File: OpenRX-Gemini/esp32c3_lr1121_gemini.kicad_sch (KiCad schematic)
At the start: 42 parts, among them T1 0900PC16J0042001E, U1 ESP32-C3FH4, U2 TLV75533PDQNR, U3 RFX2401C, U4 LR1121IMLTRT, U5 OW2EL89CENUXFMYLC-32M, X1 CJ17-400001010B20

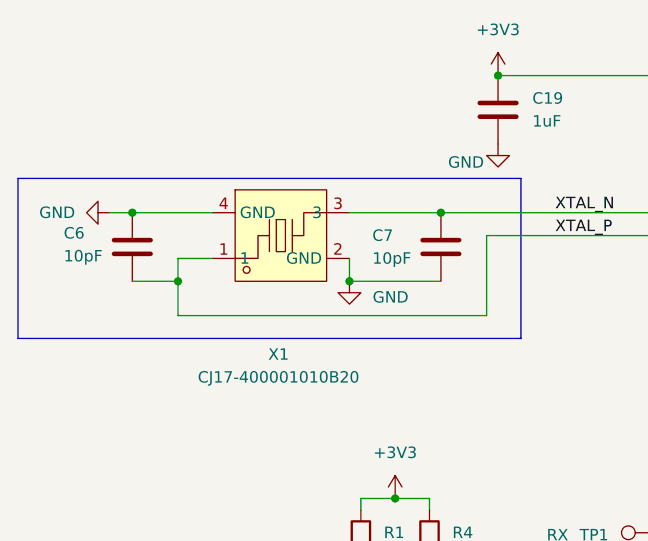
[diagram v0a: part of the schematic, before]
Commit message: Fix Gemini crystal load caps to 18pF (C62164), matching Lite and Mono
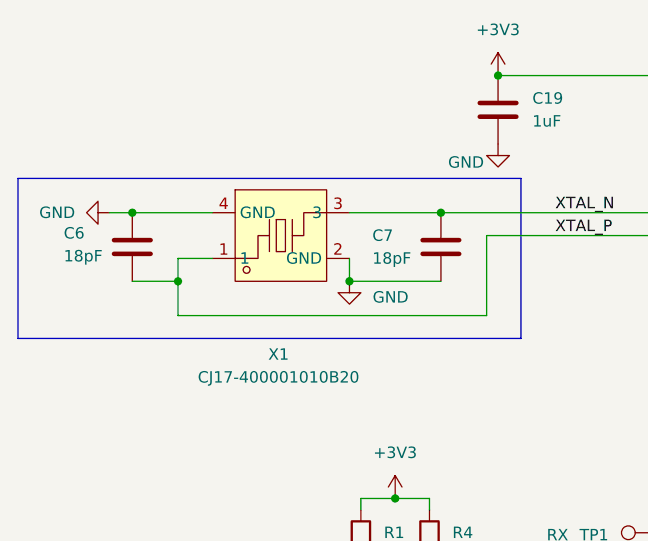
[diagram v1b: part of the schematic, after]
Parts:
- C1, C2, C21, C22, C23, C24, C3, C4, C5: LCSC C14858 -> C76939
- C10, C19, C26, C8, C9: LCSC C77857 -> C76935
- C25: LCSC C14856 -> C62548
- C6, C7: value 10pF -> 18pF; LCSC C14854 -> C62164
- L1: LCSC C1035 -> C6808014
- R1, R2, R3, R4: LCSC C172043 -> C106225
- R5: LCSC C25741 -> C270364

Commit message: OpenRX-Gemini: dual LR1121 schematic complete, 0 ERC errors
- Radio 1 (U4): sub-GHz via Johanson IPD → JP1 UFL
- Radio 2 (U9): 2.4GHz via RFX2401C (U10) → DEA (USB2) → JP3 UFL
- Shared SPI bus (SCK/MISO/MOSI), separate NSS/IRQ/BUSY/RST per radio
- Radio 2 control: GPIO10=NSS2, GPIO9=IRQ2, GPIO1=BUSY2, GPIO0=RST2
- FEM driven by Radio 2 RFSW (DIO5→RXEN, DIO6→TXEN)
- Radio 1 DIO5/DIO6 have 100k pull-downs (disconnected from FEM)
- No LED (GPIO10 used for NSS2), no boot button (GPIO9 used for IRQ2)
- Still needs: 10k pull-up on NSS2
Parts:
- removed C25: 220pF, Capacitor_SMD:C_0201_0603Metric, symbol Device:C
- removed C26: 1uF, Capacitor_SMD:C_0201_0603Metric, symbol Device:C
- removed D1: XL-1010RGBC-WS2812B, OpenRX-Shared:LED-SMD_4P-L1.0-W1.0-TL_XL-1010RGBC-WS2812B, symbol OpenRX-Shared:XL-1010RGBC-WS2812B
- removed JP2: U.FL-R-SMT-1(80), OpenRX-Shared:RF-SMD_FRF05002-JSS103M, symbol OpenRX-Shared:U.FL-R-SMT-1(80)
- removed U3: RFX2401C, OpenRX-Shared:QFN-16_L3.0-W3.0-P0.50-BL-EP1.7, symbol OpenRX-Shared:RFX2401C
- removed USB1: DEA102700LT-6307A2, OpenRX-Shared:FILTER-SMD_4P-L1.0-W0.5-L_DEA102700LT-XXX, symbol OpenRX-Shared:DEA102700LT-6307A2
- added C13, C38: 10pF, Capacitor_SMD:C_0201_0603Metric, symbol Device:C
- added C35, C36, C37, C40: 100nF, Capacitor_SMD:C_0201_0603Metric, symbol Device:C
- added C39: 4.7uF, Capacitor_SMD:C_0402_1005Metric, symbol Device:C
- added C41: 220pF, Capacitor_SMD:C_0201_0603Metric, symbol Device:C
- added C42: 1uF, Capacitor_SMD:C_0201_0603Metric, symbol Device:C
- added JP3: U.FL-R-SMT-1(80), OpenRX-Shared:RF-SMD_FRF05002-JSS103M, symbol OpenRX-Shared:U.FL-R-SMT-1(80)
- added L2: 24nH, Inductor_SMD:L_0201_0603Metric, symbol Device:L
- added L4: 10uH, Inductor_SMD:L_0603_1608Metric, symbol Device:L
- added R12, R6: 220R, Resistor_SMD:R_0201_0603Metric, symbol Device:R
- added R13, R14, R15, R16, R7: 100k, Resistor_SMD:R_0201_0603Metric, symbol Device:R
- added U10: RFX2401C, OpenRX-Shared:QFN-16_L3.0-W3.0-P0.50-BL-EP1.7, symbol OpenRX-Shared:RFX2401C
- added U8: OW2EL89CENUXFMYLC-32M, OpenRX-Shared:OSC-SMD_4P-L3.2-W2.5-BL, symbol OpenRX-Shared:OW2EL89CENUXFMYLC-32M
- added U9: LR1121IMLTRT, OpenRX-Shared:QFN-32_L5.0-W5.0-P0.50-BL-EP3.7, symbol OpenRX-Shared:LR1121IMLTRT
- added USB2: DEA102700LT-6307A2, OpenRX-Shared:FILTER-SMD_4P-L1.0-W0.5-L_DEA102700LT-XXX, symbol OpenRX-Shared:DEA102700LT-6307A2
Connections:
- net +3V3: now also C35.1, C40.2, C41.1, C42.1, L4.2, U10.14 (VDD), U10.16 (VDD), U9.15 (VBAT), U9.2 (VBAT_RF)
- net GND: now also C35.2, C36.1, C39.2, C40.1, C41.2, C42.2, JP3.2 (GND), JP3.3 (GND), R13.1, R14.1, R15.1, R16.1, R7.1, U10.1 (GND), U10.11 (GND), U10.12 (GND), U10.15 (GND), U10.17 (EP), U10.2 (GND), U10.3 (GND), U10.7 (GND), U10.8 (GND), U10.9 (GND), U8.1 (GND), U8.2 (GND), U9.13 (GND), U9.33 (EP), USB2.2 (GND), USB2.4 (GND)
- net MISO: now also U9.21 (DIO4)
- net MOSI: now also U9.22 (DIO3)
- net RXEN: now also U10.6 (RXEN), U9.20 (DIO5); no longer U4.20 (DIO5)
- net SCK: now also U9.23 (DIO2)
- net TXEN: now also U10.5 (TXEN), U9.19 (DIO6); no longer U4.19 (DIO6)
- net XTAL_P: now also L2.2; no longer C6.1, X1.1
- net RST2: now reaches U1.4 (XTAL_32K_P)
- net RST2: now also U9.6 (NRESET)
- net BUSY2: now reaches U1.5 (XTAL_32K_N)
- net BUSY2: now also U9.25 (DIO0/BUSY)
- net at U4.11 (DIO7): now also R7.2
- net at U5.3 (OUTPUT): now also R6.2; no longer U4.4 (XTA)
- net CHIP_BOOT renamed IRQ
- net IRQ: now also U9.9 (DIO9)
- net LED renamed NSS2
- net NSS2: now also U9.24 (DIO1)
- new net: C39.1, U9.1 (VR_PA)
- new net: C13.1, R6.1
- new net: U10.10 (ANT), USB2.1 (IN)
- new net: JP3.1 (SIG), USB2.3 (OUT)
- new net: R12.2, U8.3 (OUTPUT)
- new net: C37.1, U8.4 (VDD)
- new net: C6.1, L2.1, X1.1
- new net: R13.2, U9.11 (DIO7)
- new net: L4.1, U9.14 (DCC_SW)
- new net: C38.1, R12.1
- new net: U10.4 (TXRX), U9.26 (RFIO_HF)
- new net: C37.2, U9.3 (VTCXO)
- new net: R15.2, U4.19 (DIO6)
- new net: R16.2, U4.20 (DIO5)
- new net: C13.2, U4.4 (XTA)
- new net: C38.2, U9.4 (XTA)
- new net: R14.2, U9.10 (DIO8)
- new net: C36.2, U9.12 (VREG)
- no-connect marks 22 -> 31

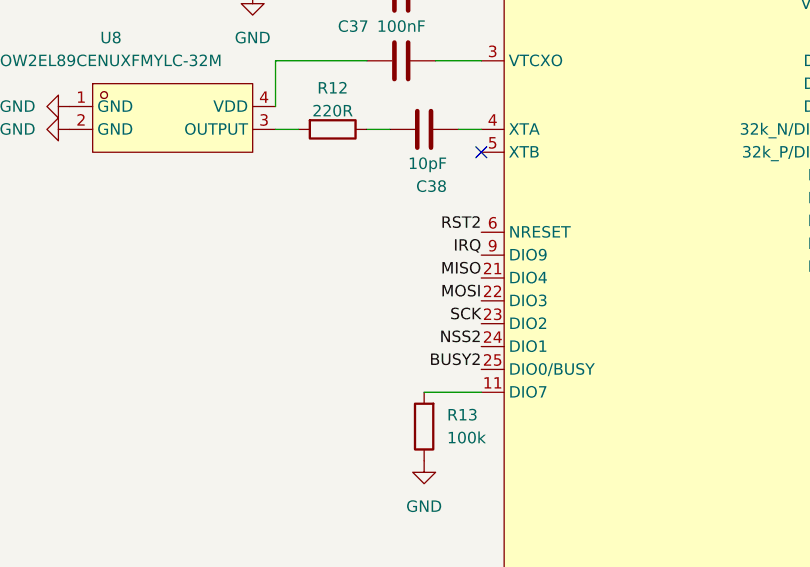
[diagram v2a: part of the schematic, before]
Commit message: Swap all solder pads to 1.2x2.0mm rounded (25%) across Lite, Mono, Gemini
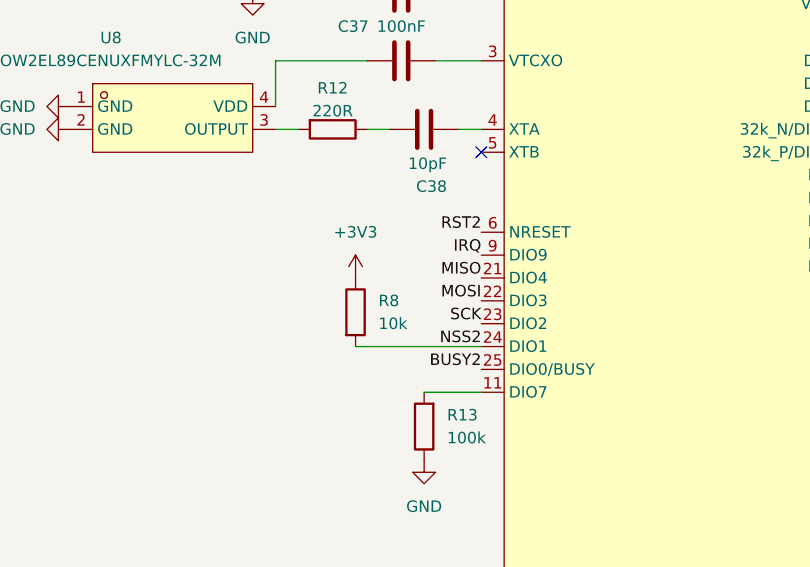
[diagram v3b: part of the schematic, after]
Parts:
- added R8: 10k, Resistor_SMD:R_0201_0603Metric, symbol Device:R
- TP1, TP2, TP3, TP4: footprint OpenRX-Shared:SolderPad_1.0x1.5mm -> OpenRX-Shared:SolderPad_1.2x2.0mm
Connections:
- net +3V3: now also R8.1
- net NSS2: now also R8.2
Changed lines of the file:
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@@
 	(wire
 		(pts
+			(xy 73.66 189.23) (xy 87.63 189.23)
+		)
+		(stroke
+			(width 0)
+			(type default)
+		)
+	)
+	(wire
+		(pts
 			(xy 189.23 114.3) (xy 190.5 114.3)
 		)
@@
 	)
 	(symbol
+		(lib_id "Device:R")
+		(at 73.66 185.42 0)
+		(unit 1)
+		(body_style 1)
+		(exclude_from_sim no)
+		(in_bom yes)
+		(on_board yes)
+		(in_pos_files yes)
+		(dnp no)
+		(fields_autoplaced yes)
+		(property "Reference" "R8"
+			(at 76.2 184.1499 0)
+			(show_name no)
+			(do_not_autoplace no)
+			(effects
+				(font
+					(size 1.27 1.27)
+				)
+				(justify left)
+			)
+		)
+		(property "Value" "10k"
+			(at 76.2 186.6899 0)
+			(show_name no)
+			(do_not_autoplace no)
+			(effects
+				(font
+					(size 1.27 1.27)
+				)
+				(justify left)
+			)
+		)
+		(property "Footprint" "Resistor_SMD:R_0201_0603Metric"
+			(at 71.882 185.42 90)
+			(hide yes)
+			(show_name no)
+			(do_not_autoplace no)
+			(effects
+				(font
+					(size 1.27 1.27)
+				)
+			)
+		)
+		(property "Datasheet" ""
+			(at 73.66 185.42 0)
+			(hide yes)
+			(show_name no)
+			(do_not_autoplace no)
+			(effects
+				(font
+					(size 1.27 1.27)
+				)
+			)
+		)
+		(property "Description" "Resistor"
+			(at 73.66 185.42 0)
+			(hide yes)
+			(show_name no)
+			(do_not_autoplace no)
+			(effects
+				(font
+					(size 1.27 1.27)
+				)
+			)
+		)
+		(property "LCSC" "C106225"
+			(at -73.66 95.25 0)
+			(hide yes)
+			(show_name no)
+			(do_not_autoplace no)
+			(effects
+				(font
+					(size 1.27 1.27)
+				)
+			)
+		)
+		(pin "2"
+		)
+		(pin "1"
+		)
+		(instances
+			(project "OpenRX-Gemini"
+				(path "/c2d3e4f5-a6b7-8901-cdef-234567890abc/a1b2c3d4-e5f6-7890-abcd-ef0123456789"
+					(reference "R8")
+					(unit 1)
+				)
+			)
+		)
+	)
+	(symbol
 		(lib_id "power:GND")
 		(at 215.9 203.2 0)
@@
 	)
 	(symbol
+		(lib_id "power:+3V3")
+		(at 73.66 181.61 0)
+		(unit 1)
+		(body_style 1)
+		(exclude_from_sim no)
+		(in_bom yes)
+		(on_board yes)
+		(in_pos_files yes)
+		(dnp no)
+		(fields_autoplaced yes)
+		(property "Reference" "#PWR010"
+			(at 73.66 185.42 0)
+			(hide yes)
+			(show_name no)
+			(do_not_autoplace no)
+			(effects
+				(font
+					(size 1.27 1.27)
+				)
+			)
+		)
+		(property "Value" "+3V3"
+			(at 73.66 176.53 0)
+			(show_name no)
+			(do_not_autoplace no)
+			(effects
+				(font
+					(size 1.27 1.27)
+				)
+			)
+		)
+		(property "Footprint" ""
+			(at 73.66 181.61 0)
+			(hide yes)
+			(show_name no)
+			(do_not_autoplace no)
+			(effects
+				(font
+					(size 1.27 1.27)
+				)
+			)
+		)
+		(property "Datasheet" ""
+			(at 73.66 181.61 0)
+			(hide yes)
+			(show_name no)
+			(do_not_autoplace no)
+			(effects
+				(font
+					(size 1.27 1.27)
+				)
+			)
+		)
+		(property "Description" "Power symbol creates a global label with name \"+3V3\""
+			(at 73.66 181.61 0)
+			(hide yes)
+			(show_name no)
+			(do_not_autoplace no)
+			(effects
+				(font
+					(size 1.27 1.27)
+				)
+			)
+		)
+		(property "LCSC" "C19213"
+			(at -73.66 95.25 0)
+			(hide yes)
+			(show_name no)
+			(do_not_autoplace no)
+			(effects
+				(font
+					(size 1.27 1.27)
+				)
+			)
+		)
+		(pin "1"
+		)
+		(instances
+			(project "OpenRX-Gemini"
+				(path "/c2d3e4f5-a6b7-8901-cdef-234567890abc/a1b2c3d4-e5f6-7890-abcd-ef0123456789"
+					(reference "#PWR010")
+					(unit 1)
+				)
+			)
+		)
+	)
+	(symbol
 		(lib_id "Device:C")
 		(at 189.23 25.4 0)
@@
 			)
 		)
-		(property "Footprint" "OpenRX-Shared:SolderPad_1.0x1.5mm"
+		(property "Footprint" "OpenRX-Shared:SolderPad_1.2x2.0mm"
 			(at 161.29 109.22 0)
 			(hide yes)
@@
 			)
 		)
-		(property "Footprint" "OpenRX-Shared:SolderPad_1.0x1.5mm"
+		(property "Footprint" "OpenRX-Shared:SolderPad_1.2x2.0mm"
 			(at 161.29 99.06 0)
 			(hide yes)
@@
 			)
 		)
-		(property "Footprint" "OpenRX-Shared:SolderPad_1.0x1.5mm"
+		(property "Footprint" "OpenRX-Shared:SolderPad_1.2x2.0mm"
 			(at 91.44 67.31 0)
 			(hide yes)
@@
 			)
 		)
-		(property "Footprint" "OpenRX-Shared:SolderPad_1.0x1.5mm"
+		(property "Footprint" "OpenRX-Shared:SolderPad_1.2x2.0mm"
 			(at 91.44 64.77 0)
 			(hide yes)

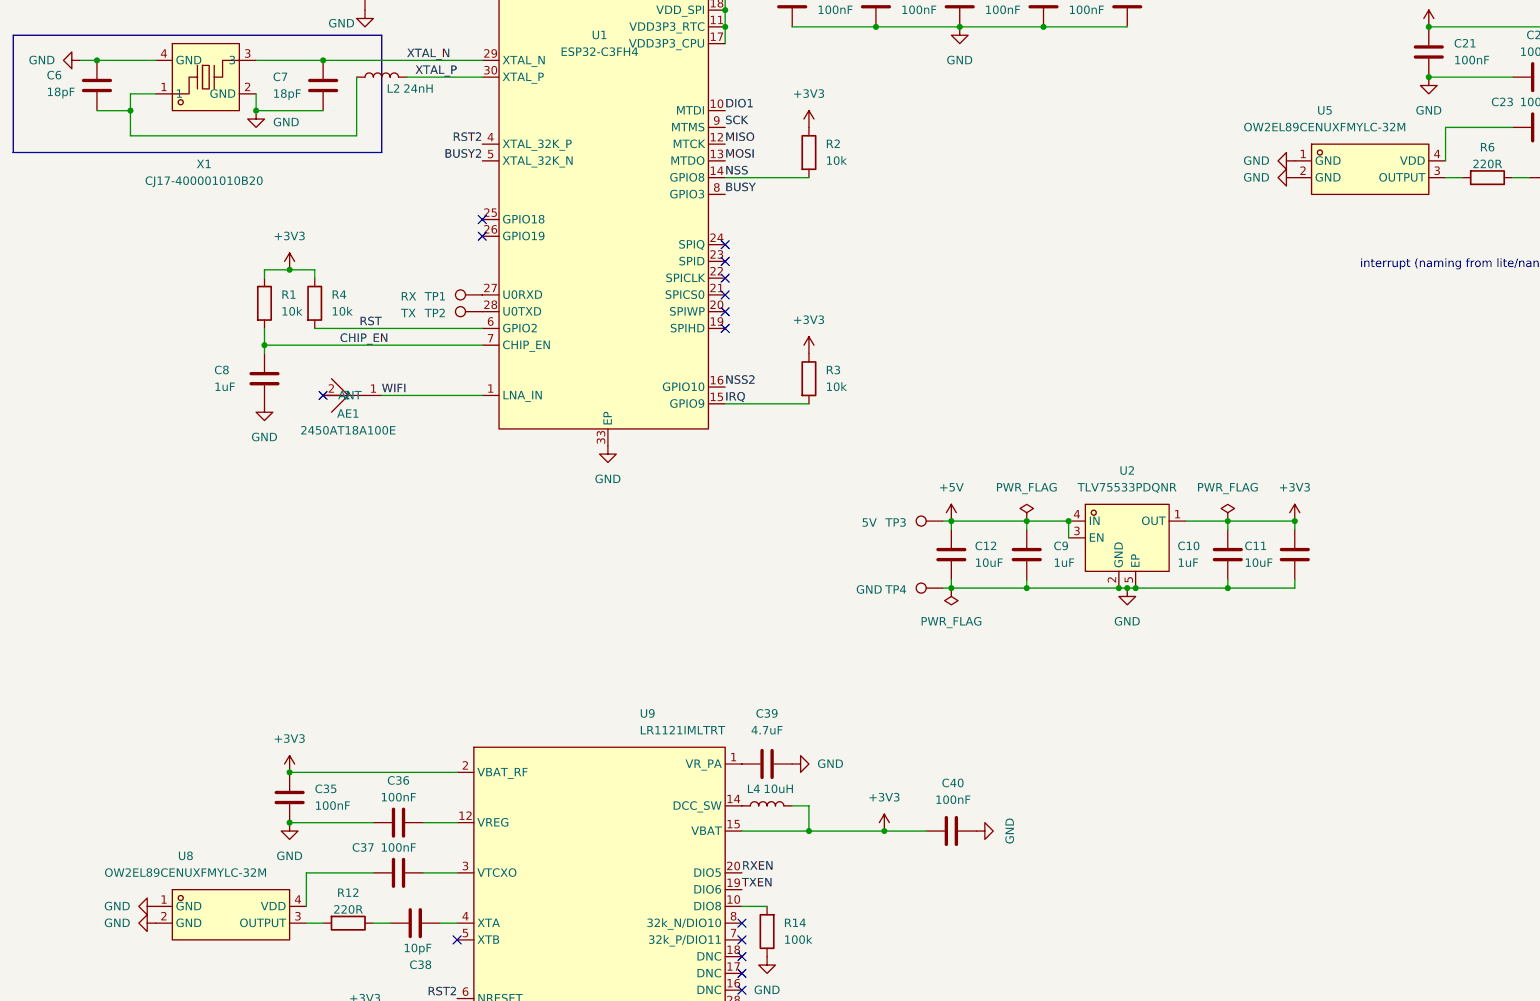
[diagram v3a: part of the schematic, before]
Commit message: Swap 32MHz TCXO to smaller 2016 package (C22381772)
OW2EL89 (3225, 3.2x2.5mm) → OW7EL89 (2016, 2.0x1.6mm)
Same YXC family, same pinout, same specs. Saves 1.2x0.9mm per TCXO.
Affects Mono (1x) and Gemini (2x).
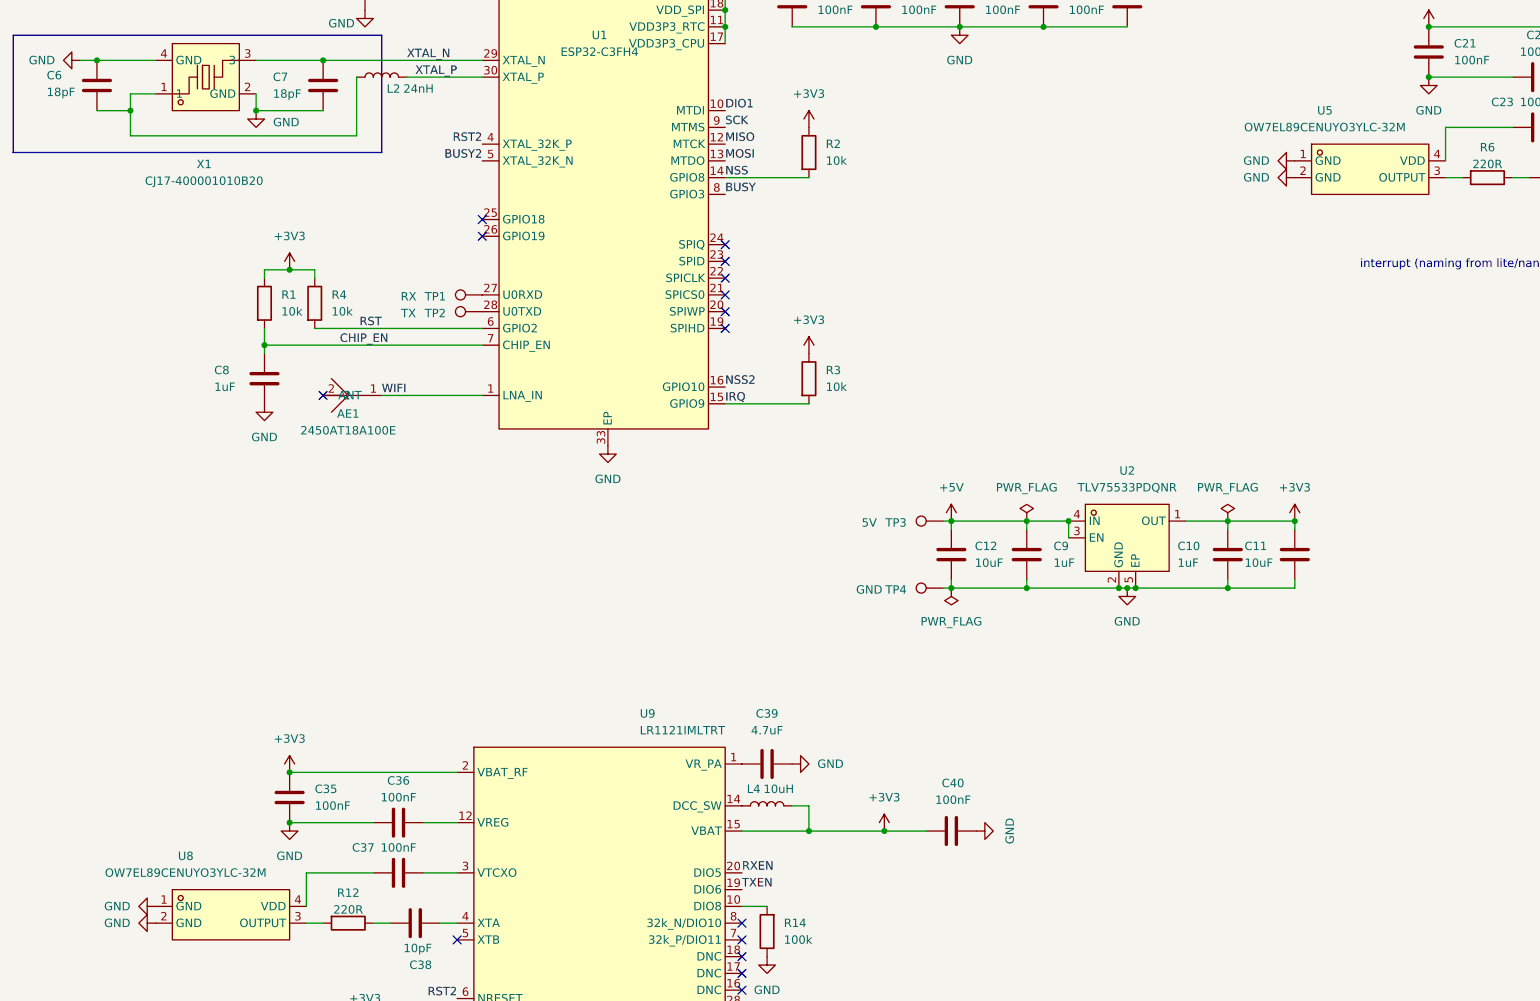
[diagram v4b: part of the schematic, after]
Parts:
- U5, U8: value OW2EL89CENUXFMYLC-32M -> OW7EL89CENUYO3YLC-32M; footprint OpenRX-Shared:OSC-SMD_4P-L3.2-W2.5-BL -> OpenRX-Shared:OSC-SMD_4P-L2.0-W1.6-BL_TXC_7Z; symbol OpenRX-Shared:OW2EL89CENUXFMYLC-32M -> OpenRX-Shared:OW7EL89CENUYO3YLC-32M; LCSC C22434888 -> C22381772; LCSC Part C22434888 -> C22381772
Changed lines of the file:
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@@
 	)
 	(symbol
-		(lib_id "OpenRX-Shared:OW2EL89CENUXFMYLC-32M")
+		(lib_id "OpenRX-Shared:OW7EL89CENUYO3YLC-32M")
 		(at 53.34 163.83 0)
 		(unit 1)
@@
 			)
 		)
-		(property "Value" "OW2EL89CENUXFMYLC-32M"
+		(property "Value" "OW7EL89CENUYO3YLC-32M"
 			(at 46.482 157.48 0)
 			(show_name no)
@@
 			)
 		)
-		(property "Footprint" "OpenRX-Shared:OSC-SMD_4P-L3.2-W2.5-BL"
+		(property "Footprint" "OpenRX-Shared:OSC-SMD_4P-L2.0-W1.6-BL_TXC_7Z"
 			(at 53.34 172.72 0)
 			(hide yes)
@@
 			)
 		)
-		(property "LCSC Part" "C22434888"
+		(property "LCSC Part" "C22381772"
 			(at 53.34 175.26 0)
 			(hide yes)
@@
 			)
 		)
-		(property "LCSC" "C22434888"
+		(property "LCSC" "C22381772"
 			(at -179.07 105.41 0)
 			(hide yes)
@@
 	)
 	(symbol
-		(lib_id "OpenRX-Shared:OW2EL89CENUXFMYLC-32M")
+		(lib_id "OpenRX-Shared:OW7EL89CENUYO3YLC-32M")
 		(at 226.06 50.8 0)
 		(unit 1)
@@
 			)
 		)
-		(property "Value" "OW2EL89CENUXFMYLC-32M"
+		(property "Value" "OW7EL89CENUYO3YLC-32M"
 			(at 219.202 44.45 0)
 			(show_name no)
@@
 			)
 		)
-		(property "Footprint" "OpenRX-Shared:OSC-SMD_4P-L3.2-W2.5-BL"
+		(property "Footprint" "OpenRX-Shared:OSC-SMD_4P-L2.0-W1.6-BL_TXC_7Z"
 			(at 226.06 59.69 0)
 			(hide yes)
@@
 			)
 		)
-		(property "LCSC Part" "C22434888"
+		(property "LCSC Part" "C22381772"
 			(at 226.06 62.23 0)
 			(hide yes)
@@
 			)
 		)
-		(property "LCSC" "C22434888"
+		(property "LCSC" "C22381772"
 			(at -6.35 -7.62 0)
 			(hide yes)
